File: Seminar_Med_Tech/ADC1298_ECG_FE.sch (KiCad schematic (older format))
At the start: 52 parts

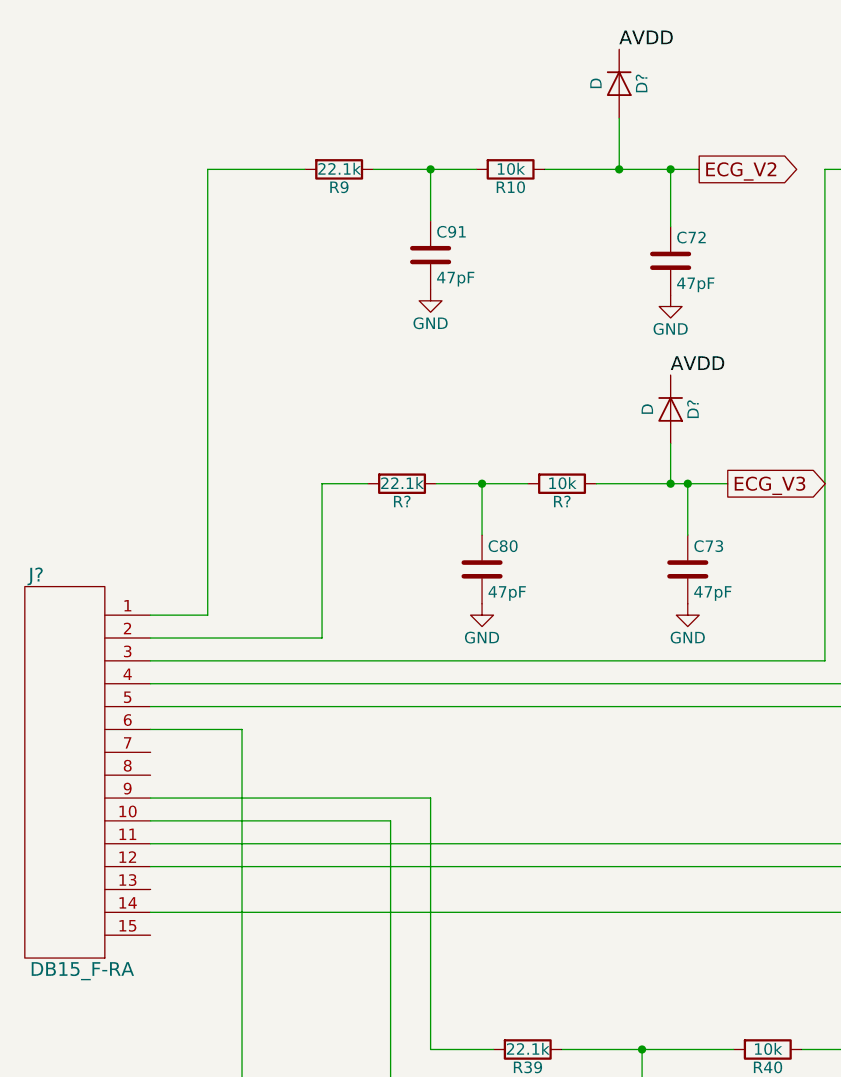
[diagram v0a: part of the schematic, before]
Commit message: ADS1298 updated
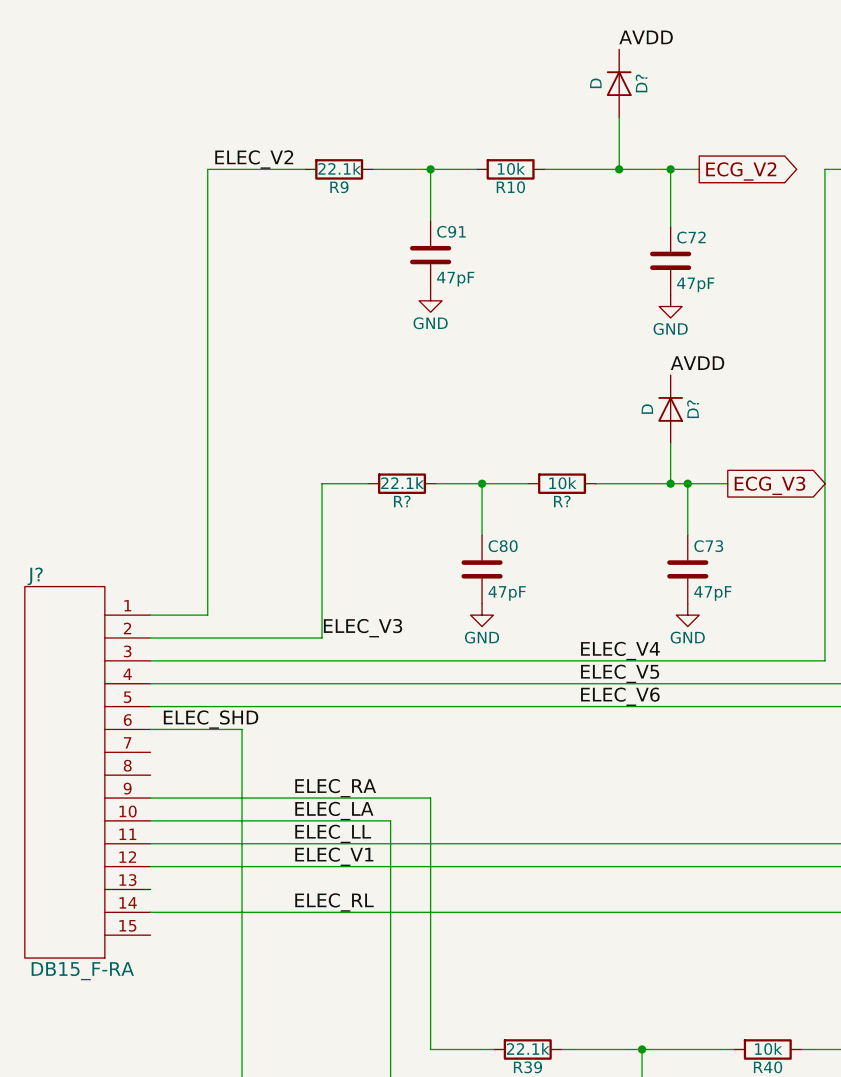
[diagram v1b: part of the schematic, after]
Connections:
- net ELEC_V2: now reaches J?.1, R9.2
- net ELEC_LA: now reaches J?.10, R43.2
- net ELEC_LL: now reaches J?.11, R33.2
- net ELEC_V1: now reaches J?.12, R29.2
- net ELEC_RL: now reaches J?.14, R37.2
- net ELEC_V3: now reaches J?.2~, R?.2
- net ELEC_V4: now reaches J?.3~, R17.2
- net ELEC_V5: now reaches J?.4~, R21.2
- net ELEC_V6: now reaches J?.5, R25.2
- net ELEC_SHD: now reaches J?.6, JP15.2
- net ELEC_RA: now reaches J?.9, R39.2
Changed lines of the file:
@@
 LIBS:ECG_Power_Supplies-cache
 LIBS:Connectors-cache
+LIBS:ADC1298_ECG_FE-cache
 EELAYER 25 0
 EELAYER END
@@
 Text GLabel 3750 1350 2    60   Output ~ 0
 ECG_V2
+Text Label 1625 1350 0    60   ~ 0
+ELEC_V2
+Text Label 2100 3400 0    60   ~ 0
+ELEC_V3
+Text Label 3225 3500 0    60   ~ 0
+ELEC_V4
+Text Label 3225 3600 0    60   ~ 0
+ELEC_V5
+Text Label 1400 3800 0    60   ~ 0
+ELEC_SHD
+Text Label 3225 3700 0    60   ~ 0
+ELEC_V6
+Text Label 1975 4100 0    60   ~ 0
+ELEC_RA
+Text Label 1975 4200 0    60   ~ 0
+ELEC_LA
+Text Label 1975 4300 0    60   ~ 0
+ELEC_LL
+Text Label 1975 4400 0    60   ~ 0
+ELEC_V1
+Text Label 1975 4600 0    60   ~ 0
+ELEC_RL
 $EndSCHEMATC

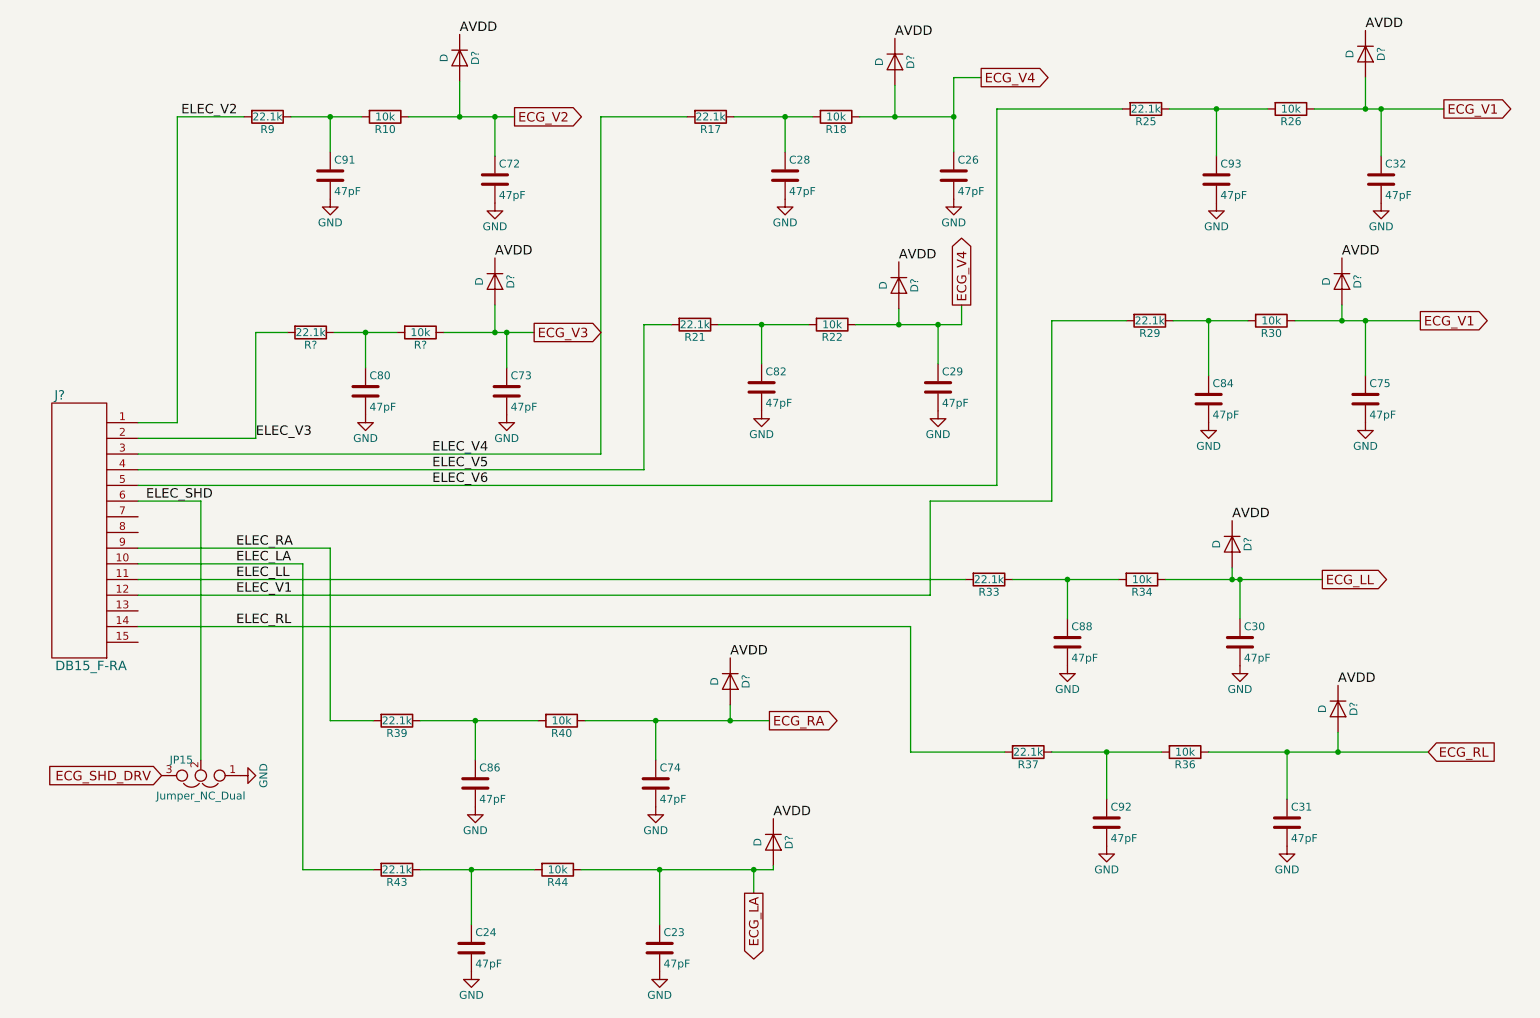
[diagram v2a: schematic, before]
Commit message: Changed labels in ADC1298_ECG_FE
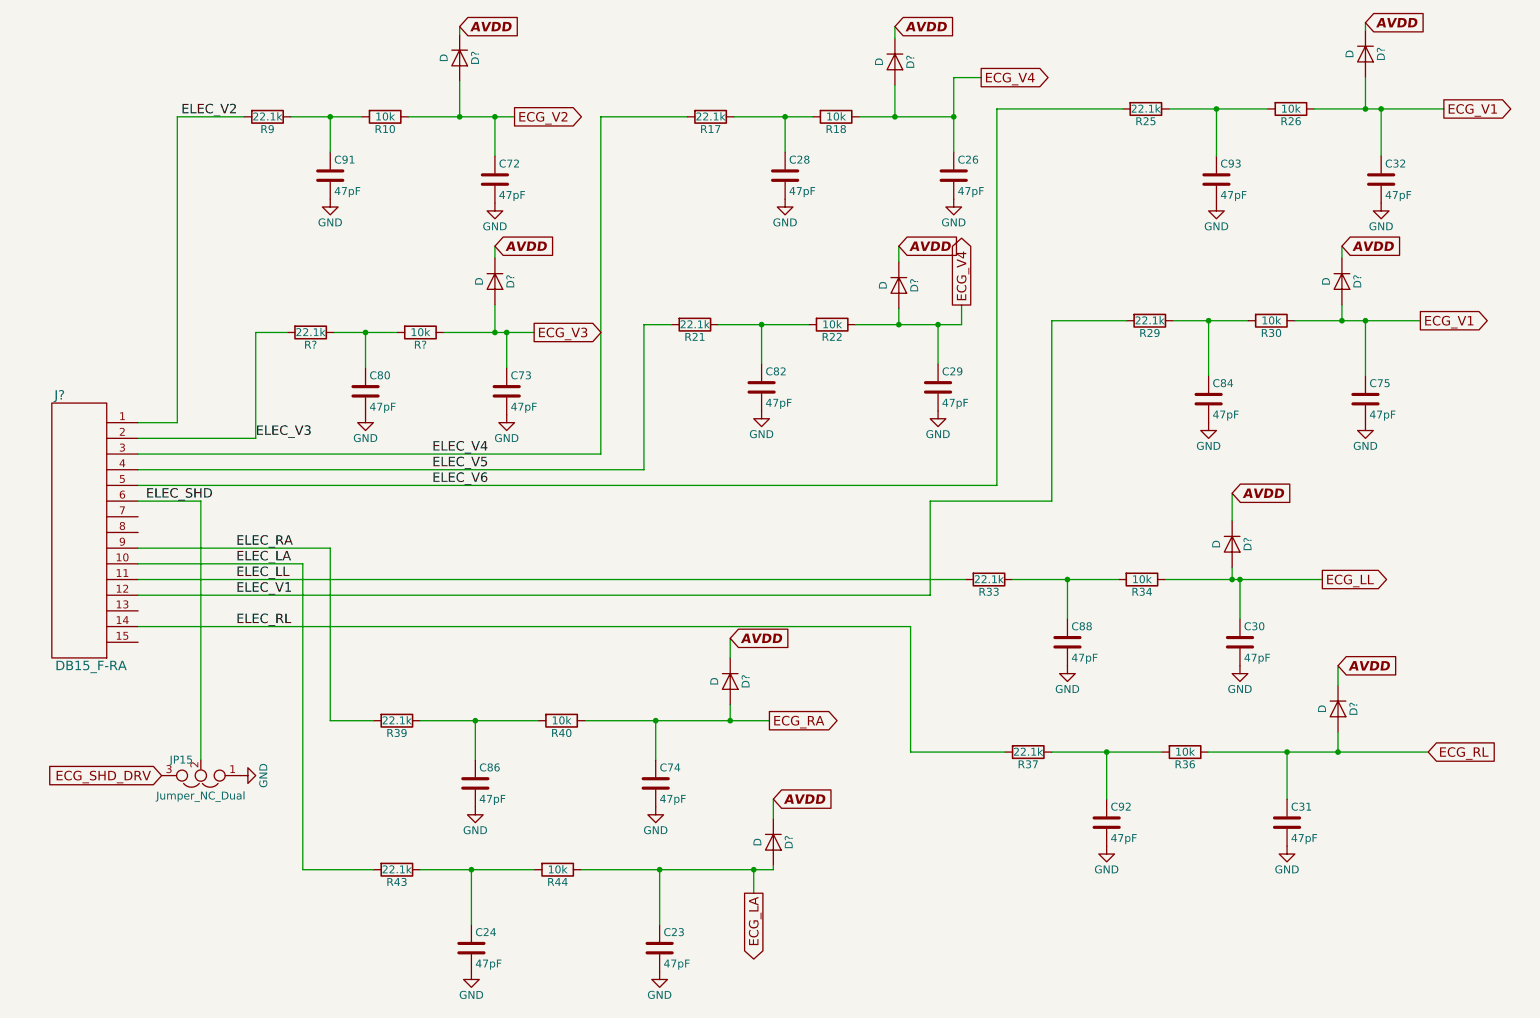
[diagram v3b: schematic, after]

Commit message: Update
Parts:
- gave numbers to parts that had none: 13
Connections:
- net ECG_V1: no longer C32.1, D10.2 (A), R26.1
- net ECG_V4: no longer C29.1, D6.2 (A), R22.1
- net GND: no longer C23.2, C24.2, C26.2, C28.2, C29.2, C30.2, C31.2, C32.2, C72.2, C73.2, C74.2, C75.2, C80.2, C82.2, C84.2, C86.2, C88.2, C91.2, C92.2, C93.2
- new net AGND: C23.2, C24.2, C26.2, C28.2, C29.2, C30.2, C31.2, C32.2, C72.2, C73.2, C74.2, C75.2, C80.2, C82.2, C84.2, C86.2, C88.2, C91.2, C92.2, C93.2
- new net ECG_V5: C29.1, D6.2 (A), R22.1
- new net ECG_V6: C32.1, D10.2 (A), R26.1
- no-connect marks 0 -> 4

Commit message: jumper
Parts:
- C23, C24, C26, C28, C29, C30, C31, C32, C72, C73, C74, C75, C80, C82, C84, C86, C88, C91, C92, C93: footprint (none) -> Capacitors_SMD:C_1206_HandSoldering
- D1, D10, D2, D3, D4, D5, D6, D7, D8, D9: footprint (none) -> Diodes_SMD:D_SC-80_HandSoldering
- J6: footprint (none) -> Pin_Headers:Pin_Header_Straight_1x15_Pitch2.54mm
- JP15: footprint (none) -> jumper:jumper1x3
- R10, R13, R14, R17, R18, R21, R22, R25, R26, R29, R30, R33, R34, R36, R37, R39, R40, R43, R44, R9: footprint (none) -> Resistors_SMD:R_0805_HandSoldering

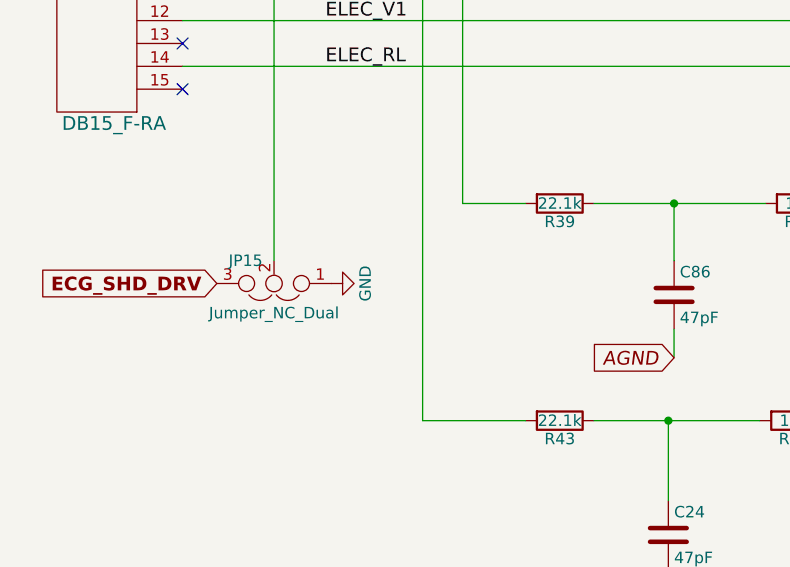
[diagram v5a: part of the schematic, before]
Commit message: Updated Bauteilliste and Schaltbild
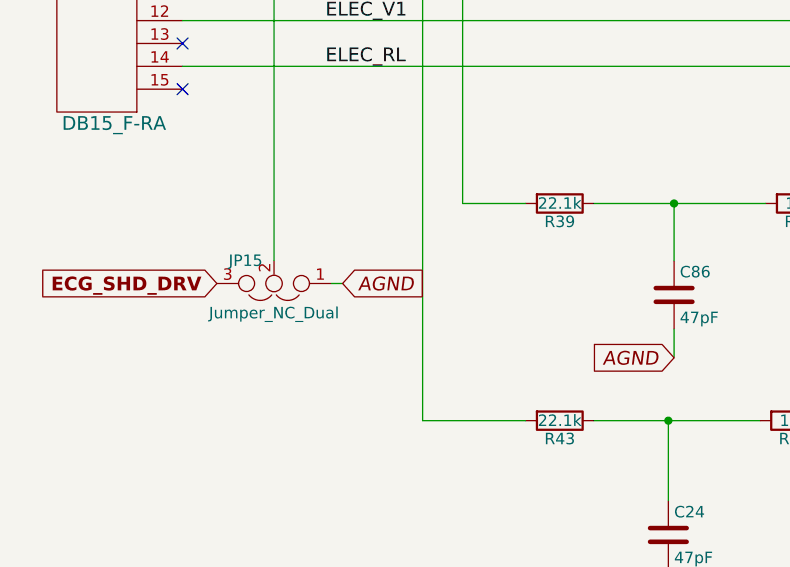
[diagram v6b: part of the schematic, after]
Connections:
- net GND is gone; now on net AGND: JP15.1
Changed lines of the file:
@@
 	-1   0    0    1
-$EndComp
-$Comp
-L GND #PWR06
-U 1 1 5945AC6C
-P 2000 5550
-F 0 "#PWR06" H 2000 5300 50  0001 C CNN
-F 1 "GND" H 2000 5400 50  0000 C CNN
-F 2 "" H 2000 5550 50  0001 C CNN
-F 3 "" H 2000 5550 50  0001 C CNN
-	1    2000 5550
-	0    -1   -1   0
 $EndComp
 Text GLabel 1500 5550 0    60   Input ~ 12
@@
 Wire Wire Line
 	9275 1975 9275 1900
+Text GLabel 2050 5550 2    60   Input Italic 0
+AGND
+Wire Wire Line
+	2000 5550 2050 5550
 $EndSCHEMATC

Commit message: Updated
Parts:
- added J?: CONN_01X10, symbol CONN_01X10
- added J?: CONN_01X02, symbol CONN_01X02
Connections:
- net ELEC_LA: now also J?.7 (P7)
- net ELEC_LL: now also J?.8 (P8)
- net ELEC_RA: now also J?.6 (P6)
- net ELEC_RL: now also J?.10 (P10)
- net ELEC_SHD: now also J?.2 (P2)
- net ELEC_V1: now also J?.9 (P9)
- net ELEC_V2: now also J?.1 (P1)
- net ELEC_V3: now also J?.2 (P2)
- net ELEC_V4: now also J?.3 (P3)
- net ELEC_V5: now also J?.4 (P4)
- net ELEC_V6: now also J?.5 (P5)
- no-connect marks 4 -> 5
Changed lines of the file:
@@
 Text GLabel 3750 1350 2    60   Output ~ 12
 ECG_V2
-Text Label 1625 1350 0    60   ~ 0
+Text Label 1825 1350 2    60   ~ 0
 ELEC_V2
 Text Label 2100 3400 0    60   ~ 0
@@
 Text Label 3225 3600 0    60   ~ 0
 ELEC_V5
-Text Label 1400 3800 0    60   ~ 0
+Text Label 1750 3925 0    60   ~ 0
 ELEC_SHD
 Text Label 3225 3700 0    60   ~ 0
@@
 NoConn ~ 1350 4500
 NoConn ~ 1350 4700
+Text GLabel 2050 5550 2    60   Input Italic 0
+AGND
+$Comp
+L CONN_01X10 J?
+U 1 1 5947AEC5
+P 800 2100
+F 0 "J?" H 800 2650 50  0000 C CNN
+F 1 "CONN_01X10" V 900 2100 50  0000 C CNN
+F 2 "" H 800 2100 50  0001 C CNN
+F 3 "" H 800 2100 50  0001 C CNN
+	1    800  2100
+	-1   0    0    1
+$EndComp
 Wire Wire Line
 	3700 3250 3700 3325
@@
 Connection ~ 5275 6150
 Wire Wire Line
-	5275 6300 5275 6150
+	5275 6150 5275 6300
 Wire Wire Line
 	1750 3800 1750 5450
@@
 	1350 4600 6275 4600
 Wire Wire Line
-	2400 4200 1350 4200
-Wire Wire Line
-	2400 6150 2400 4200
-Wire Wire Line
-	2850 6150 2400 6150
+	1350 4200 2400 4200
+Wire Wire Line
+	2400 4200 2400 6150
+Wire Wire Line
+	2400 6150 2850 6150
 Wire Wire Line
 	2575 5200 2850 5200
@@
 	1350 4400 6400 4400
 Wire Wire Line
-	6825 1300 6825 3700
-Wire Wire Line
-	7625 1300 6825 1300
+	6825 3700 6825 1300
+Wire Wire Line
+	6825 1300 7625 1300
 Wire Wire Line
 	4575 2675 4750 2675
 Wire Wire Line
-	4575 2675 4575 3600
-Wire Wire Line
-	4575 3600 1350 3600
-Wire Wire Line
-	6825 3700 1350 3700
+	4575 3600 4575 2675
+Wire Wire Line
+	1350 3600 4575 3600
+Wire Wire Line
+	1350 3700 6825 3700
 Connection ~ 4675 6150
 Wire Wire Line
@@
 	2325 1350 2775 1350
 Wire Wire Line
-	1600 1350 2025 1350
-Wire Wire Line
-	1600 3300 1600 1350
-Wire Wire Line
-	1350 3300 1600 3300
+	1825 1350 2025 1350
+Wire Wire Line
+	1825 3300 1825 1350
+Wire Wire Line
+	1350 3300 1825 3300
 Wire Wire Line
 	2800 3250 2800 3325
@@
 Wire Wire Line
 	9275 1975 9275 1900
-Text GLabel 2050 5550 2    60   Input Italic 0
-AGND
 Wire Wire Line
 	2000 5550 2050 5550
+Wire Wire Line
+	1375 3300 1375 2550
+Wire Wire Line
+	1375 2550 1000 2550
+Connection ~ 1375 3300
+Wire Wire Line
+	1000 2450 1400 2450
+Wire Wire Line
+	1400 2450 1400 3400
+Connection ~ 1400 3400
+Wire Wire Line
+	1000 2350 1425 2350
+Wire Wire Line
+	1425 2350 1425 3500
+Connection ~ 1425 3500
+Wire Wire Line
+	1000 2250 1450 2250
+Wire Wire Line
+	1450 2250 1450 3600
+Connection ~ 1450 3600
+Wire Wire Line
+	1000 2150 1475 2150
+Wire Wire Line
+	1475 2150 1475 3700
+Connection ~ 1475 3700
+Wire Wire Line
+	1000 2050 1500 2050
+Wire Wire Line
+	1500 2050 1500 4100
+Connection ~ 1500 4100
+Wire Wire Line
+	1000 1950 1525 1950
+Wire Wire Line
+	1525 1950 1525 4200
+Connection ~ 1525 4200
+Wire Wire Line
+	1000 1850 1550 1850
+Wire Wire Line
+	1550 1850 1550 4300
+Connection ~ 1550 4300
+Wire Wire Line
+	1000 1750 1575 1750
+Wire Wire Line
+	1575 1750 1575 4400
+Connection ~ 1575 4400
+Wire Wire Line
+	1000 1650 1600 1650
+Wire Wire Line
+	1600 1650 1600 4600
+Connection ~ 1600 4600
+Wire Wire Line
+	900  5000 1750 5000
+Connection ~ 1750 5000
+$Comp
+L CONN_01X02 J?
+U 1 1 59492CE6
+P 700 5050
+F 0 "J?" H 700 5200 50  0000 C CNN
+F 1 "CONN_01X02" V 800 5050 50  0000 C CNN
+F 2 "" H 700 5050 50  0001 C CNN
+F 3 "" H 700 5050 50  0001 C CNN
+	1    700  5050
+	-1   0    0    1
+$EndComp
+NoConn ~ 900  5100
 $EndSCHEMATC
